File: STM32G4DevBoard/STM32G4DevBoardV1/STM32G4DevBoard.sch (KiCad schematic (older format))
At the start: 26 parts, among them J1 USB_B_Micro, J2 Conn_01x13, J3 Conn_01x13, U1 STM32G431KBTx, U2 LD3985M33R_SOT23, Y1 24MHz

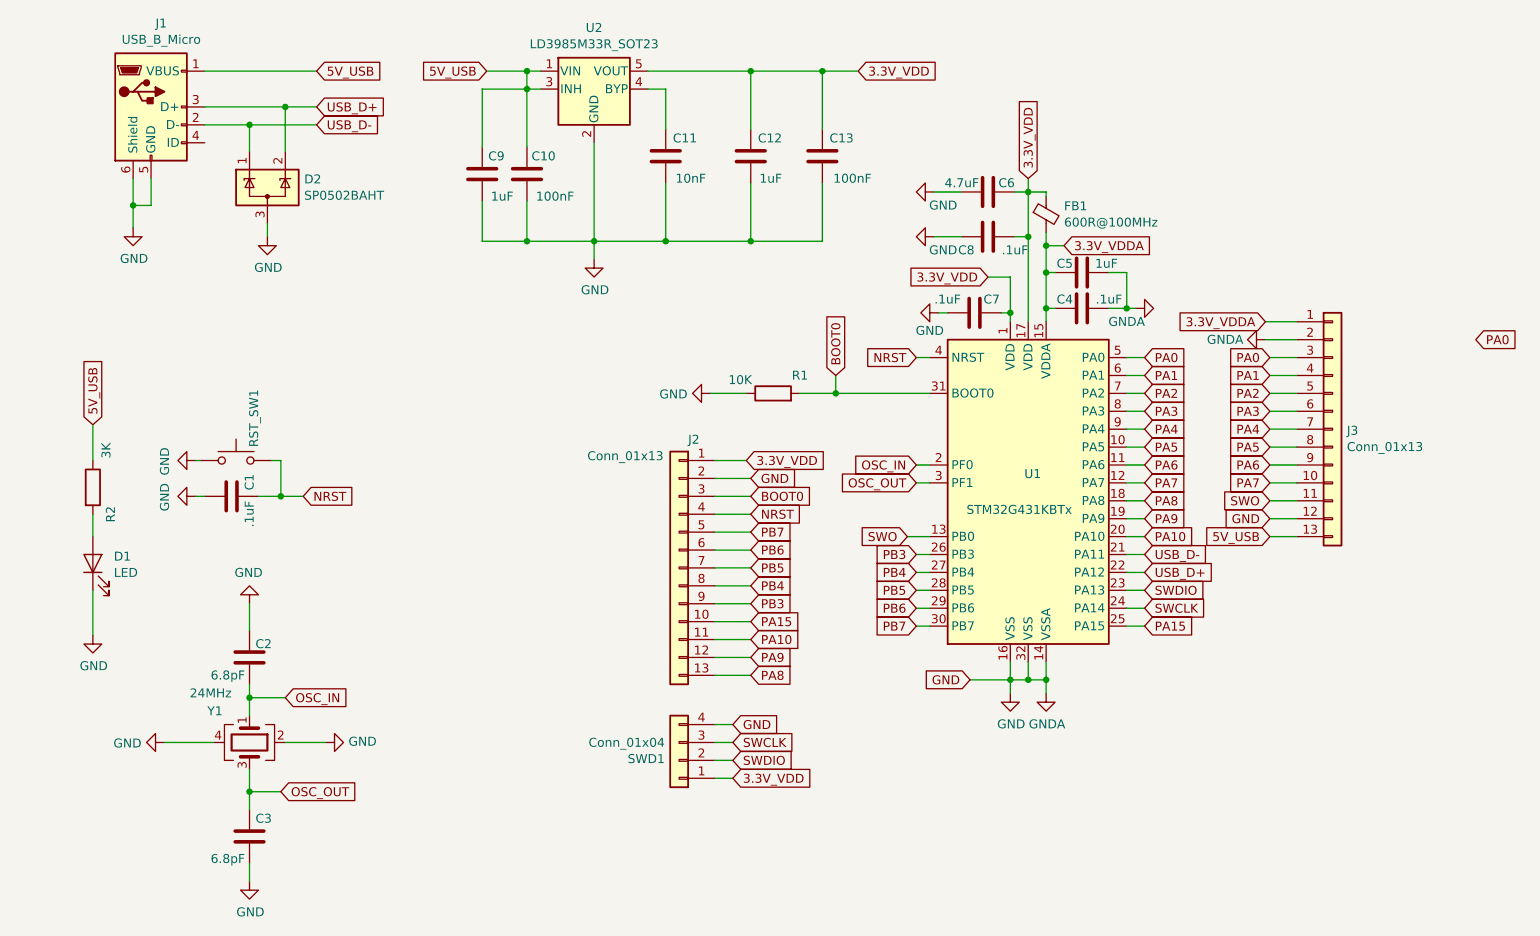
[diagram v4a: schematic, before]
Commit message: Added Ferride Beads and test LED
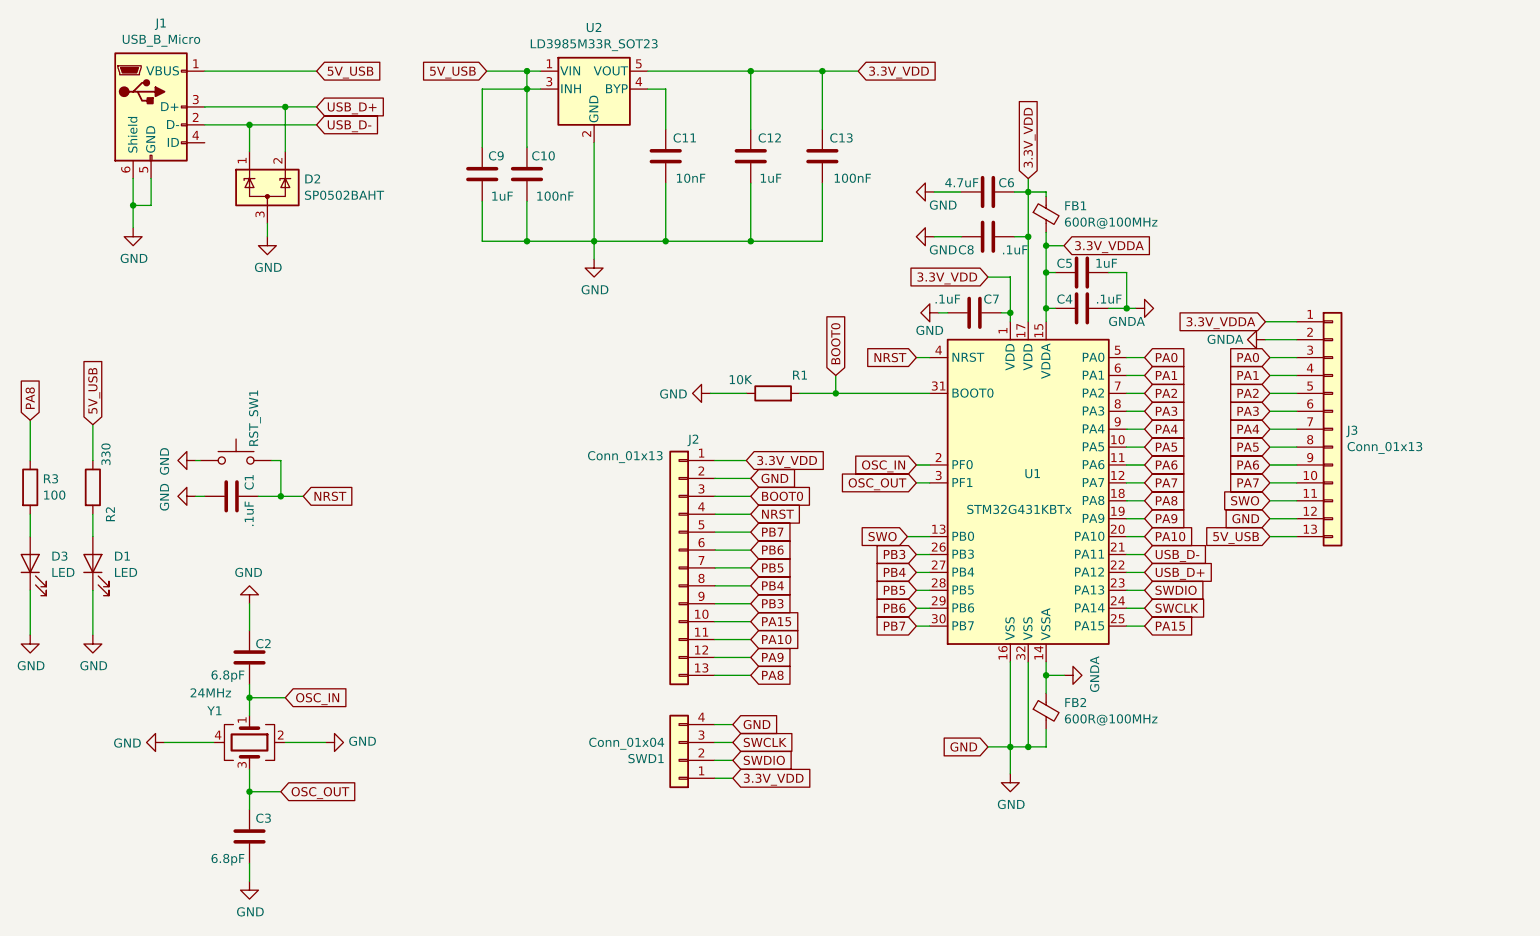
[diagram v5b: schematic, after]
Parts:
- added D3: LED, LED_SMD:LED_0603_1608Metric_Pad1.05x0.95mm_HandSolder, symbol Device:LED
- added FB2: 600R@100MHz, Inductor_SMD:L_0603_1608Metric_Pad1.05x0.95mm_HandSolder, symbol Device:Ferrite_Bead_Small
- added R3: 100, Resistor_SMD:R_0603_1608Metric_Pad1.05x0.95mm_HandSolder, symbol Device:R
- R2: value 3K -> 330
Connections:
- net GND: now also D3.1 (K), FB2.2; no longer C4.2, C5.2, J3.2 (Pin_2), U1.14 (VSSA)
- net PA8: now also R3.1
- new net: D3.2 (A), R3.2
- new net GNDA: C4.2, C5.2, FB2.1, J3.2 (Pin_2), U1.14 (VSSA)
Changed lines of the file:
@@
 Wire Wire Line
 	7100 2875 7100 3075
-Connection ~ 6550 5150
-Wire Wire Line
-	6650 5150 6650 5225
-Connection ~ 6650 5150
-Wire Wire Line
-	6650 5150 6550 5150
-$Comp
-L power:GNDA #PWR011
-U 1 1 5D71D2E4
-P 6650 5225
-F 0 "#PWR011" H 6650 4975 50  0001 C CNN
-F 1 "GNDA" H 6655 5052 50  0000 C CNN
-F 2 "" H 6650 5225 50  0001 C CNN
-F 3 "" H 6650 5225 50  0001 C CNN
-	1    6650 5225
-	1    0    0    -1
-$EndComp
-Wire Wire Line
-	6650 5050 6650 5150
-$Comp
-L power:GND #PWR010
-U 1 1 5D71CBEF
-P 6450 5225
-F 0 "#PWR010" H 6450 4975 50  0001 C CNN
-F 1 "GND" H 6455 5052 50  0000 C CNN
-F 2 "" H 6450 5225 50  0001 C CNN
-F 3 "" H 6450 5225 50  0001 C CNN
-	1    6450 5225
-	1    0    0    -1
-$EndComp
 $Comp
 L Device:R R1
@@
 Text GLabel 5925 3350 0    50   Input ~ 0
 NRST
-Wire Wire Line
-	6450 5150 6450 5225
-Connection ~ 6450 5150
-Wire Wire Line
-	6550 5150 6450 5150
-Wire Wire Line
-	6550 5050 6550 5150
-Wire Wire Line
-	6450 5050 6450 5150
+Connection ~ 6450 5525
+Wire Wire Line
+	6550 5525 6450 5525
+Wire Wire Line
+	6550 5050 6550 5525
+Wire Wire Line
+	6450 5050 6450 5525
 $Comp
 L power:GND #PWR03
@@
 P 1325 4075
 F 0 "R2" V 1425 3925 50  0000 C CNN
-F 1 "3K" V 1400 4325 50  0000 R CNN
+F 1 "330" V 1400 4325 50  0000 R CNN
 F 2 "Resistor_SMD:R_0603_1608Metric_Pad1.05x0.95mm_HandSolder" V 1255 4075 50  0001 C CNN
 F 3 "~" H 1325 4075 50  0001 C CNN
@@
 GND
 Wire Wire Line
-	6450 5150 6225 5150
-Text GLabel 6225 5150 0    50   Input ~ 0
+	6450 5525 6325 5525
+Text GLabel 6325 5525 0    50   Input ~ 0
 GND
 Text GLabel 4900 5600 2    50   Input ~ 0
 SWDIO
-Text GLabel 9050 3250 2    50   Input ~ 0
-PA0
 Text GLabel 7900 3350 0    50   Input ~ 0
 PA0
@@
 Wire Wire Line
 	8050 4050 7900 4050
+Wire Wire Line
+	6650 5050 6650 5125
+$Comp
+L power:GND #PWR010
+U 1 1 5D71CBEF
+P 6450 5675
+F 0 "#PWR010" H 6450 5425 50  0001 C CNN
+F 1 "GND" H 6455 5502 50  0000 C CNN
+F 2 "" H 6450 5675 50  0001 C CNN
+F 3 "" H 6450 5675 50  0001 C CNN
+	1    6450 5675
+	1    0    0    -1
+$EndComp
+Wire Wire Line
+	6450 5525 6450 5675
+$Comp
+L Device:R R3
+U 1 1 5DF9BCFF
+P 975 4075
+F 0 "R3" H 1045 4121 50  0000 L CNN
+F 1 "100" H 1045 4030 50  0000 L CNN
+F 2 "Resistor_SMD:R_0603_1608Metric_Pad1.05x0.95mm_HandSolder" V 905 4075 50  0001 C CNN
+F 3 "~" H 975 4075 50  0001 C CNN
+	1    975  4075
+	1    0    0    -1
+$EndComp
+Text GLabel 975  3700 1    50   Input ~ 0
+PA8
+Wire Wire Line
+	975  4350 975  4225
+$Comp
+L Device:LED D3
+U 1 1 5DFAD0DC
+P 975 4500
+F 0 "D3" V 1014 4383 50  0000 R CNN
+F 1 "LED" V 923 4383 50  0000 R CNN
+F 2 "LED_SMD:LED_0603_1608Metric_Pad1.05x0.95mm_HandSolder" H 975 4500 50  0001 C CNN
+F 3 "~" H 975 4500 50  0001 C CNN
+	1    975  4500
+	0    -1   -1   0
+$EndComp
+Wire Wire Line
+	975  3925 975  3700
+$Comp
+L power:GND #PWR012
+U 1 1 5DFB4B46
+P 975 4900
+F 0 "#PWR012" H 975 4650 50  0001 C CNN
+F 1 "GND" H 980 4727 50  0000 C CNN
+F 2 "" H 975 4900 50  0001 C CNN
+F 3 "" H 975 4900 50  0001 C CNN
+	1    975  4900
+	1    0    0    -1
+$EndComp
+Wire Wire Line
+	975  4650 975  4900
+$Comp
+L power:GNDA #PWR011
+U 1 1 5E04D426
+P 6750 5125
+F 0 "#PWR011" H 6750 4875 50  0001 C CNN
+F 1 "GNDA" H 6755 4952 50  0000 C CNN
+F 2 "" H 6750 5125 50  0001 C CNN
+F 3 "" H 6750 5125 50  0001 C CNN
+	1    6750 5125
+	0    -1   -1   0
+$EndComp
+Wire Wire Line
+	6750 5125 6650 5125
+Connection ~ 6650 5125
+Wire Wire Line
+	6650 5125 6650 5225
+Wire Wire Line
+	6550 5525 6650 5525
+Wire Wire Line
+	6650 5525 6650 5425
+Connection ~ 6550 5525
+$Comp
+L Device:Ferrite_Bead_Small FB2
+U 1 1 5E07169E
+P 6650 5325
+F 0 "FB2" H 6750 5371 50  0000 L CNN
+F 1 "600R@100MHz" H 6750 5280 50  0000 L CNN
+F 2 "Inductor_SMD:L_0603_1608Metric_Pad1.05x0.95mm_HandSolder" V 6580 5325 50  0001 C CNN
+F 3 "~" H 6650 5325 50  0001 C CNN
+	1    6650 5325
+	1    0    0    -1
+$EndComp
 $EndSCHEMATC
